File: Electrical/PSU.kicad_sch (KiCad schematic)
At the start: 112 parts, among them IC2 SiC437AED-T1-GE3, J15 Conn_01x03_Pin, J16 USB_C_Receptacle_USB2.0, Q10 2N7002, Q8 2N7002, Q9 2N7002, SW1 SW_Push, U13 HT7533, U14 CH224Q_C46061833, U15 SY8253ADC, U16 SY8253ADC, U6 SY8253ADC, U7 SY8253ADC

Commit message: further updates
split the ground plane for the sic437
use ethernet port that is available for purchase easily
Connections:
- net GND: no longer C1.2, C125.2, C149.2, C2.2, IC2.13 (PGND_3), IC2.16 (AGND_1), IC2.25 (AGND_2), IC2.27 (PGND_4), IC2.29 (PGND_5), IC2.3 (PGND_1), IC2.4 (PGND_2), R26.1, R39.1
- new net A_GND: IC2.16 (AGND_1), IC2.25 (AGND_2), R26.1, R39.1
- new net P_GND: C1.2, C125.2, C149.2, C2.2, IC2.13 (PGND_3), IC2.27 (PGND_4), IC2.29 (PGND_5), IC2.3 (PGND_1), IC2.4 (PGND_2)
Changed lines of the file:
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@@
 			)
 		)
-		(property "Value" "GND"
+		(property "Value" "P_GND"
 			(at 408.94 191.7699 90)
 			(show_name no)
@@
 			)
 		)
-		(property "Value" "GND"
-			(at 368.3 194.3099 90)
+		(property "Value" "P_GND"
+			(at 370.84 190.5 90)
 			(show_name no)
 			(do_not_autoplace no)
@@
 					(size 1.27 1.27)
 				)
-				(justify right)
 			)
 		)
@@
 			)
 		)
-		(property "Value" "GND"
+		(property "Value" "A_GND"
 			(at 455.93 156.2099 90)
 			(show_name no)
@@
 			)
 		)
-		(property "Value" "GND"
+		(property "Value" "P_GND"
 			(at 408.94 196.8499 90)
 			(show_name no)
@@
 			)
 		)
-		(property "Value" "GND"
-			(at 349.25 176.53 0)
+		(property "Value" "P_GND"
+			(at 351.79 172.7199 0)
 			(show_name no)
 			(do_not_autoplace no)
@@
 					(size 1.27 1.27)
 				)
+				(justify left)
 			)
 		)
@@
 			)
 		)
-		(property "Value" "GND"
-			(at 368.3 168.9099 90)
+		(property "Value" "P_GND"
+			(at 370.84 165.1 90)
 			(show_name no)
 			(do_not_autoplace no)
@@
 					(size 1.27 1.27)
 				)
-				(justify right)
 			)
 		)
@@
 			)
 		)
-		(property "Value" "GND"
+		(property "Value" "A_GND"
 			(at 408.94 186.6899 90)
 			(show_name no)
@@
 			)
 		)
-		(property "Value" "GND"
-			(at 368.3 171.4499 90)
+		(property "Value" "P_GND"
+			(at 370.84 167.64 90)
 			(show_name no)
 			(do_not_autoplace no)
@@
 					(size 1.27 1.27)
 				)
-				(justify right)
 			)
 		)
@@
 			)
 		)
-		(property "Value" "GND"
-			(at 355.6 191.7699 90)
+		(property "Value" "P_GND"
+			(at 358.14 187.96 90)
 			(show_name no)
 			(do_not_autoplace no)
@@
 					(size 1.27 1.27)
 				)
-				(justify right)
 			)
 		)

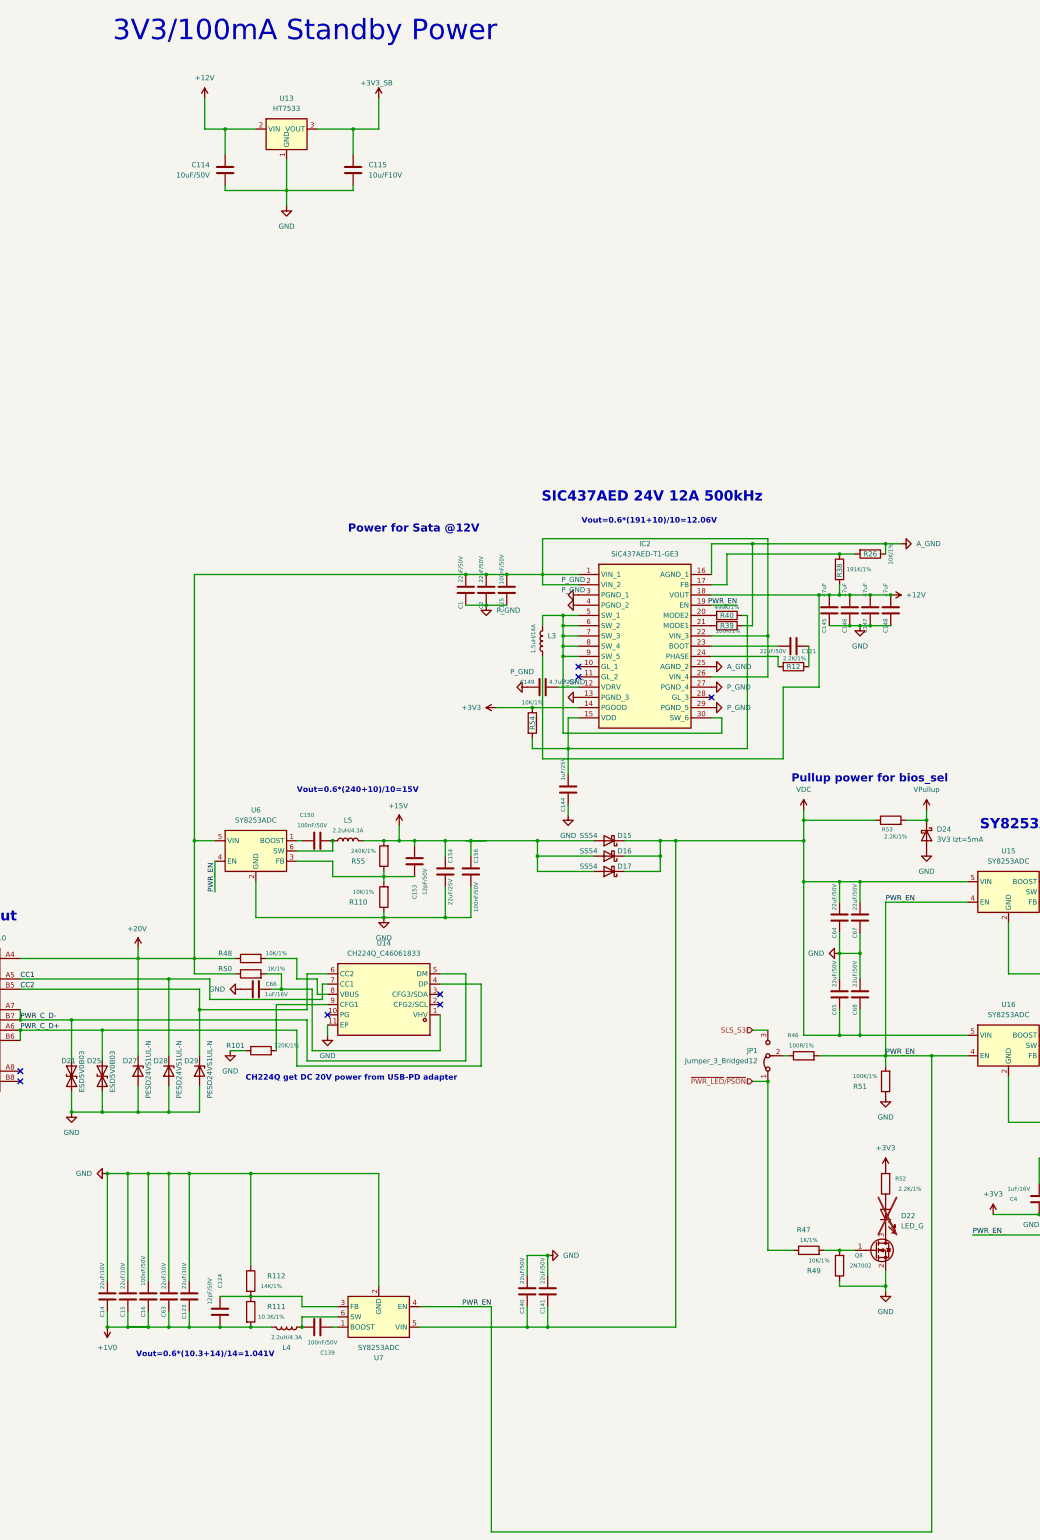
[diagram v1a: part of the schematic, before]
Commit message: add some fixes from initial prototype and fix 1v0 regulator
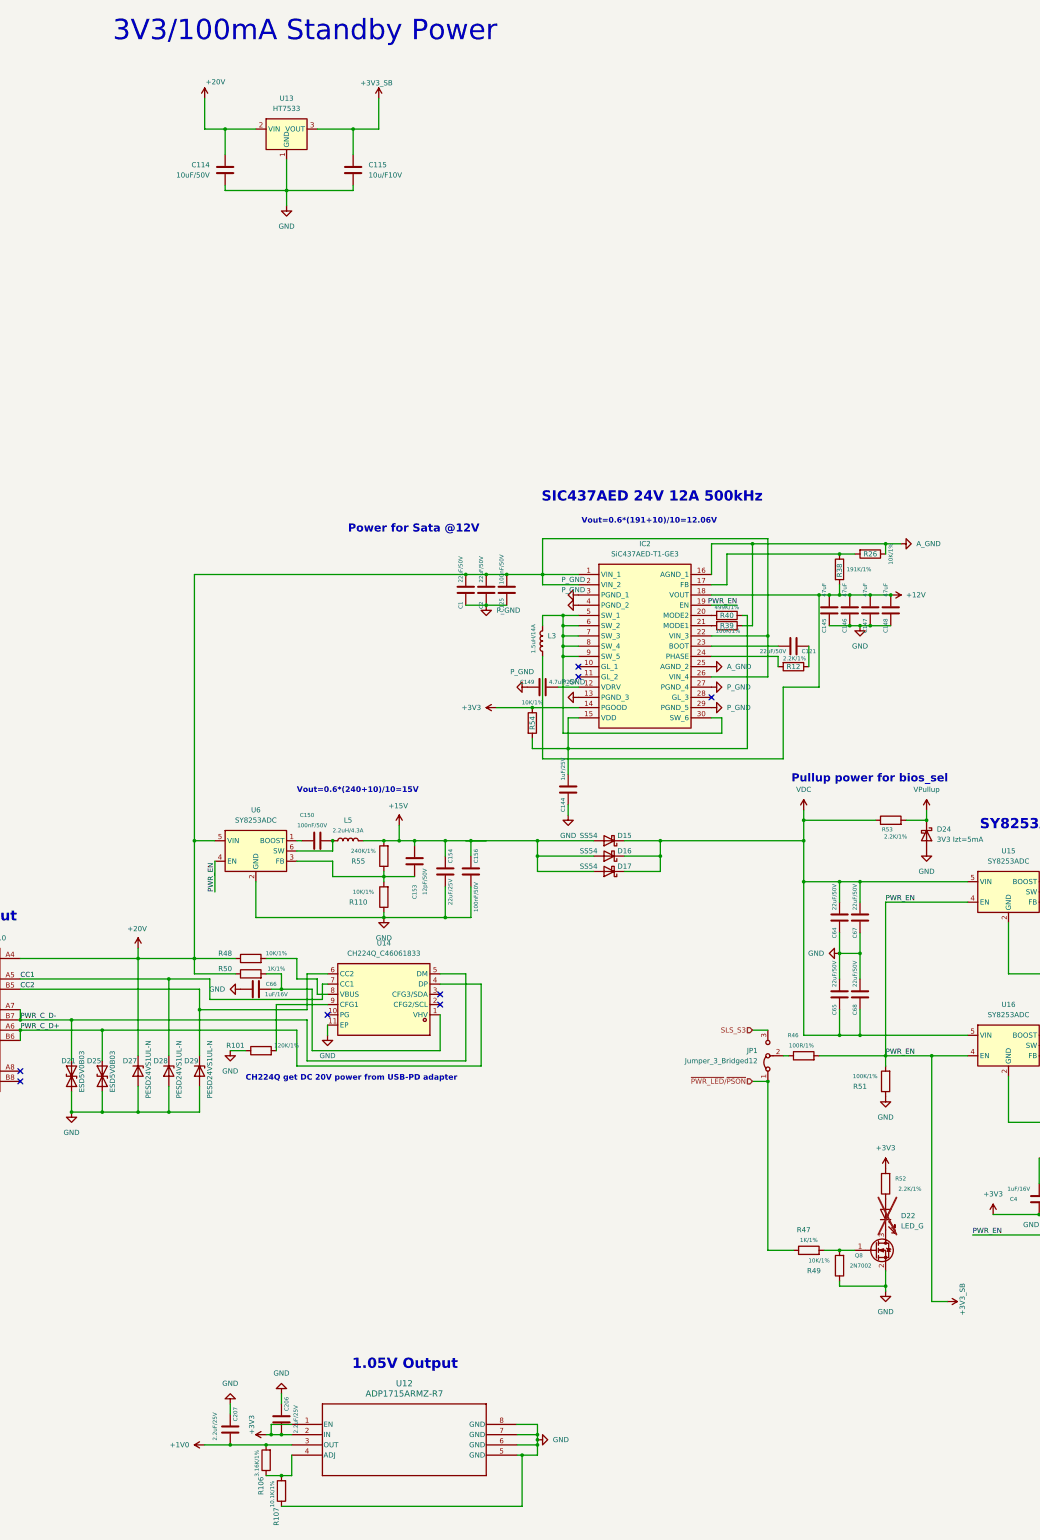
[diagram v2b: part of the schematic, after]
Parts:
- removed C123, C14, C15, C63: 22uF/10V, A_HDJ_Library:C_0603_1608Metric, symbol Device:C
- removed C124: 12pF/50V, Capacitor_SMD:C_0402_1005Metric, symbol Device:C
- removed C139, C16: 100nF/50V, A_HDJ_Library:C_0402_1005Metric, symbol Device:C
- removed C140, C141: 22uF/50V, A_HDJ_Library:C_0603_1608Metric, symbol Device:C
- removed L4: 2.2uH/4.3A, inductor-2:SPM4010-4020, symbol Device:L
- removed R111: 10.3K/1%, A_HDJ_Library:R_0402_1005Metric, symbol Device:R
- removed R112: 14K/1%, A_HDJ_Library:R_0402_1005Metric, symbol Device:R
- removed U7: SY8253ADC, Package_TO_SOT_SMD:TSOT-23-6, symbol Regulator_Switching:LM2734X
- added C206, C207: 2.2uF/25V, Capacitor_SMD:C_0603_1608Metric_Pad1.08x0.95mm_HandSolder, symbol Device:C
- added R106: 3.16K/1%, Resistor_SMD:R_0201_0603Metric_Pad0.64x0.40mm_HandSolder, symbol Device:R
- added R107: 10.1K/1%, Resistor_SMD:R_0201_0603Metric_Pad0.64x0.40mm_HandSolder, symbol Device:R
- added U12: ADP1715ARMZ-R7, 1v ldo:RM_8_ADI, symbol 1v ldo:ADP1715ARMZ-R7
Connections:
- net PWR_EN is gone; now on net +3V3_SB: IC2.19 (EN), R46.2, R51.2, U10.3 (EN), U15.4 (EN), U16.4 (EN), U6.4 (EN), U9.3 (EN)
- net +12V: no longer C114.1, U13.2 (VIN)
- net +1V0: now also C207.1, R106.2, U12.3 (OUT)
- net +20V: now also C114.1, U13.2 (VIN)
- net +3V3: now also C206.1, U12.1 (EN), U12.2 (IN)
- net GND: now also C206.2, C207.2, R107.1, U12.5 (GND), U12.6 (GND), U12.7 (GND), U12.8 (GND)
- new net: R106.1, R107.2, U12.4 (ADJ)
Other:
- note added: "1.05V Output"
- note removed: "Vout=0.6*(10.3+14)/14=1.041V"

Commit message: better implementation of 0.95v
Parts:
- removed C3, C4: 1uF/16V, A_HDJ_Library:C_0402_1005Metric, symbol Device:C
- removed R66: CR0402-FX-9531GLF, RESC1005X40N, symbol 9.53k resis:CR0402-FX-9531GLF
- removed R70: CRCW040250K0FKED, RESC1005X40N, symbol 50k resis:CRCW040250K0FKED
- removed U10: (no value), Package_TO_SOT_SMD:SOT-23-5, symbol ldo:BL8079AGCB5TR
- added C110: 22uF/10V, A_HDJ_Library:C_0603_1608Metric, symbol Device:C
- added C90: 10uF/50V, Capacitor_SMD:C_0402_1005Metric, symbol Device:C
- added C91: 100nF/50V, Capacitor_SMD:C_0402_1005Metric, symbol Device:C
- added L6: 2.2uH/4.3A, inductor-2:SPM4010-4020, symbol Device:L
- added R108: 2.37K/1%, Resistor_SMD:R_0201_0603Metric_Pad0.64x0.40mm_HandSolder, symbol Device:R
- added R109: 10.1K/1%, Resistor_SMD:R_0201_0603Metric_Pad0.64x0.40mm_HandSolder, symbol Device:R
- added U7: TPS562201DDCR, DDC0006A_N, symbol 0.95v buck:TPS562201DDCR
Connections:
- net +0V9: now also L6.2
- net +5V: now also C90.2, U7.3 (VIN), U7.5 (EN)
- net GND: now also C110.1, C90.1, R109.1, U7.1 (GND)
- new net: C91.1, U7.6 (VBST)
- new net: C110.2, C91.2, L6.1, R108.2, U7.2 (SW)
- new net: R108.1, R109.2, U7.4 (VFB)
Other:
- note added: "0.95v Output"

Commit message: Update Board Further
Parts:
- removed D24: 3V3 Izt=5mA, Diode_SMD:D_SOD-923, symbol Device:D_Schottky
- removed R51: 100K/1%, A_HDJ_Library:R_0402_1005Metric, symbol Device:R
- removed R53: 2.2K/1%, Resistor_SMD:R_0402_1005Metric, symbol Device:R
- removed U13: HT7533, Package_TO_SOT_SMD:SOT-89-3, symbol Regulator_Linear:HT75xx-1-SOT89
- added U13: NCP718xSN300, Package_TO_SOT_SMD:SOT-23-5, symbol Regulator_Linear:NCP718xSN300
- R26: value 10K/1% -> 1.0K/1%
- R38: value 191K/1% -> 19.1K/1%
- R39: value 100K/1% -> 200K/1%
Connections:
- net P_GND is gone; now on net sic-gnd: C1.2, C125.2, C149.2, C2.2, IC2.13 (PGND_3), IC2.27 (PGND_4), IC2.29 (PGND_5), IC2.3 (PGND_1), IC2.4 (PGND_2)
- net +20V: now also U13.1 (IN), U13.3 (EN)
- net +3V3: no longer IC2.14 (PGOOD), R54.1
- net +3V3_SB: now also U13.5 (OUT)
- net GND: now also U13.2 (GND)
- net A_GND renamed sic-gnd
- net VDC: no longer names the net of C64.1, C65.2, C67.1, C68.2, D15.1 (K), D16.1 (K), D17.1 (K), U15.5 (VIN), U16.5 (VIN)
- new net: IC2.14 (PGOOD), R54.1
